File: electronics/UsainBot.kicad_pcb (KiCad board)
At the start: 4 copper layers, 155 x 164.9 mm, 340 parts, among them J101 TYPE-C-31-M-12, J102 Pack 2S - AMASS MR30, J103 Montage vertical ESC (prototy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, J201 TC2030-IDC-FP, J301 Moteur Faulhaber + IE2, J351 Moteur Faulhaber + IE2, J601 OLED SSD1306 I2C, J701 Module OTA (ESP32-C3), M1 Faulhaber 1524T006SR + IE2 + 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, M2 Faulhaber 1524T006SR + IE2 + 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, M3 Turbine_EDF27_dessus, Q101 AO3400A, Q102 AO4407A, Q103 AO4407A, Q104 AO3400A, Q401 AO3400A, Q402 AO3400A, Q501 AO3400A, Q521 AO3400A, Q541 AO3400A, Q601 AO3400A, Q602 AO3400A, Q701 SI2301CDS, Q702 AO3400A, SW101 MARCHE / ARRET, SW601 SKRHABE010, SW602 START, SW603 RESET, U101 USBLC6-2SC6, U102 BQ25887RGER, U103 TPS62933DRLR, U105 PCA9685PW, U201 STM32H723ZGT6, U301 DRV8874PWPR, U351 DRV8874PWPR, U401 ITR8307/S17/TR8(B), U402 ITR8307/S17/TR8(B), U403 ITR8307/S17/TR8(B), U404 ITR8307/S17/TR8(B), U405 ITR8307/S17/TR8(B), U406 ITR8307/S17/TR8(B), U407 ITR8307/S17/TR8(B), U408 ITR8307/S17/TR8(B), U409 ITR8307/S17/TR8(B), U410 ITR8307/S17/TR8(B), U411 ITR8307/S17/TR8(B), U412 ITR8307/S17/TR8(B), U501 TLV9064, U502 TLV9064, U503 LSM6DSOTR, U504 TLV9064, U701 W25Q128JVSIQ, Y201 25 MHz / 10 ppm

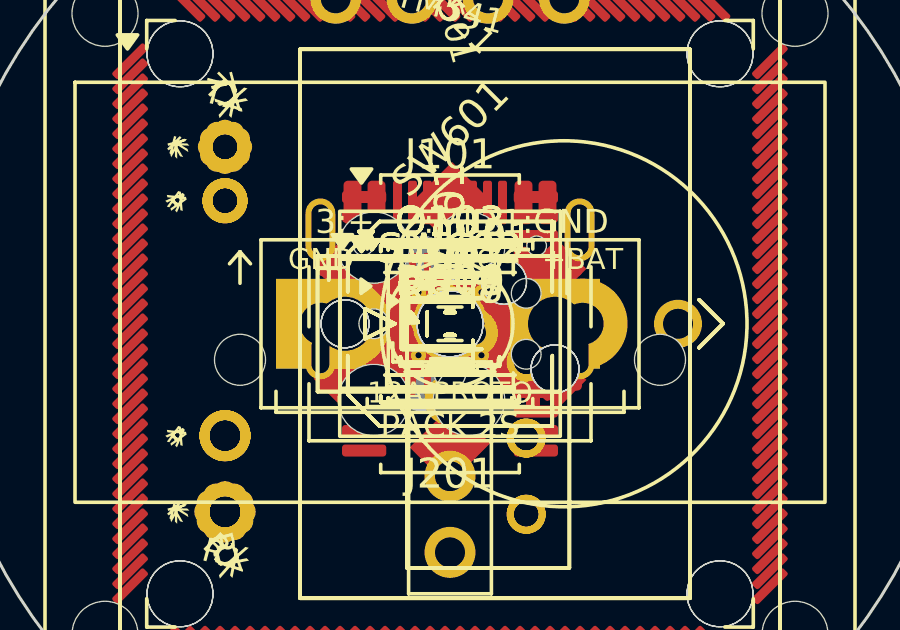
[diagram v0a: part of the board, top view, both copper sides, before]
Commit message: Alimente les codeurs en 5 V, renomme les paires USB et passe les résistances des LED en 0603
- Codeurs IE2 : U302 TPS70950 sur VBAT (EN sur +3V3, le 5 V suit le MCU
  dont les entrées FT_h ne tolèrent 5 V qu'alimentées), C310 1 µF et
  C311 4,7 µF ; net /Moteurs/ENC_5V vers J301.4 et J351.4, classe
  ALIM_LOGIQUE. Symbole Pacabot:TPS70950DBV ajouté à la bibliothèque.
- Paires USB : USB_D_P/N et /Alimentation/USB_C_D_P/N, reconnues comme
  paires par KiCad et par le routeur de paires du fork.
- R615, R617, R618 en 0603 à 390/560/560 ohms (≈ 10 mA, ≤ 50 mW à 7,3 V) ;
  R615 et R618 recalées, D609 décalée de 0,25 mm, R617 déplacée à côté
  de R306 faute de place pour une 0603 près de D608.

Schéma et carte concordent pastille par pastille (netlist KiCad 10.0.1) ;
ERC 0, DRC sans nouvelle violation. Détail dans rules-review/README.md.

Co-Authored-By: Claude Opus 5.5 <noreply@anthropic.com>
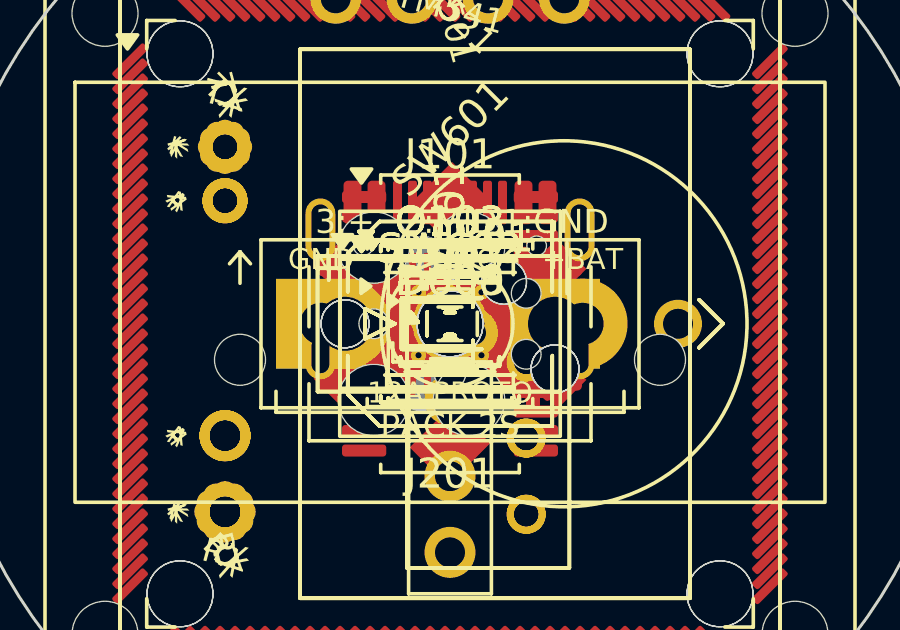
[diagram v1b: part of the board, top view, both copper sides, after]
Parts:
- added C310: 1uF, Capacitor_SMD:C_0402_1005Metric, F.Cu at (0.00, 0.00)
- added C311: 4.7uF, Capacitor_SMD:C_0603_1608Metric, F.Cu at (0.00, 0.00)
- added U302: TPS70950DBVR, Package_TO_SOT_SMD:SOT-23-5, F.Cu at (0.00, 0.00)
- R615: value 220R -> 390R; footprint Resistor_SMD:R_0402_1005Metric -> Resistor_SMD:R_0603_1608Metric
- R617, R618: value 300R -> 560R; footprint Resistor_SMD:R_0402_1005Metric -> Resistor_SMD:R_0603_1608Metric
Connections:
- net /Alimentation/USB_DM_C renamed /Alimentation/USB_C_D_N
- net /Alimentation/USB_DP_C renamed /Alimentation/USB_C_D_P
- net USB_DM renamed USB_D_N
- net USB_DP renamed USB_D_P
- J301 pad 4: +3V3 -> /Moteurs/ENC_5V
- J351 pad 4: +3V3 -> /Moteurs/ENC_5V

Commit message: Ramène la carte au format KiCad 10.0 stable
Le fork 10.99 (autorouteur) enregistrait la carte au format 20260901,
que KiCad 10.0.x refuse d'ouvrir. tools/to_kicad10.py la réécrit au
format 20260206 : position des 343 empreintes de (transform (translate)
(rotate) (scale 1 1)) vers (at x y r), et retrait des réglages que 10.0
ne connaît pas (spec_frequency, dielectric_model, zone_defaults, pngdpi,
pngantialias).

Vérifié : fichier de placement identique, Gerber F.Cu/B.Cu/F.Mask/B.Mask
identiques entre le fork sur l'original et 10.0.1 sur la carte convertie ;
le contour ne diffère que par la finesse de découpe des deux Bézier.
DRC 10.0.1 : mêmes violations hors règles propres au fork, 499 liaisons à
router, 3 écarts de champs de parité inchangés. Le fork ouvre toujours la
carte convertie.

Co-Authored-By: Claude Opus 5.5 <noreply@anthropic.com>
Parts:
- moved R432 346.5 mm to (222.8, 265.3), turned to -120.285 degrees
- moved C412 345.8 mm to (223.9, 263.6), turned to 59.7151 degrees
- moved R412 343.9 mm to (220.4, 263.9), turned to 59.7151 degrees
- moved D412 343.5 mm to (223.0, 261.4), turned to 59.7151 degrees
- moved U412 343.5 mm to (223.0, 261.4), turned to -30.2849 degrees
- moved R431 343.0 mm to (207.8, 272.9), turned to -112.918 degrees
- moved R456 342.6 mm to (224.4, 258.9), turned to -120.285 degrees
- moved C411 342.0 mm to (208.6, 271.1), turned to 67.0817 degrees
- moved R411 340.6 mm to (205.2, 271.8), turned to 67.0817 degrees
- moved D411 339.7 mm to (207.4, 269.0), turned to 67.0817 degrees
- moved U411 339.7 mm to (207.4, 269.0), turned to -22.9183 degrees
- moved R430 338.3 mm to (192.0, 278.6), turned to -105.552 degrees
- moved R455 338.3 mm to (208.5, 266.4), turned to -112.918 degrees
- moved C410 337.0 mm to (192.5, 276.6), turned to 74.4483 degrees
- moved R410 336.2 mm to (189.3, 277.8), turned to 74.4483 degrees
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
